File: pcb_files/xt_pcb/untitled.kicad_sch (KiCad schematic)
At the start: 181 parts, among them SW1 SW_Push, SW10 SW_Push, SW11 SW_Push, SW12 SW_Push, SW13 SW_Push, SW14 SW_Push, SW15 SW_Push, SW16 SW_Push, SW17 SW_Push, SW19 SW_Push, SW2 SW_Push, SW20 SW_Push, SW21 SW_Push, SW22 SW_Push, SW23 SW_Push, SW24 SW_Push, SW25 SW_Push, SW26 SW_Push, SW27 SW_Push, SW28 SW_Push, SW29 SW_Push, SW3 SW_Push, SW30 SW_Push, SW31 SW_Push, SW32 SW_Push, SW33 SW_Push, SW34 SW_Push, SW35 SW_Push, SW36 SW_Push, SW37 SW_Push, SW38 SW_Push, SW39 SW_Push, SW4 SW_Push, SW40 SW_Push, SW41 SW_Push, SW42 SW_Push, SW43 SW_Push, SW44 SW_Push, SW45 SW_Push, SW46 SW_Push, SW47 SW_Push, SW48 SW_Push, SW49 SW_Push, SW5 SW_Push, SW50 SW_Push, SW51 SW_Push, SW52 SW_Push, SW53 SW_Push, SW54 SW_Push, SW55 SW_Push, SW56 SW_Push, SW57 SW_Push, SW58 SW_Push, SW59 SW_Push, SW6 SW_Push, SW60 SW_Push, SW61 SW_Push, SW62 SW_Push, SW63 SW_Push, SW64 SW_Push, SW66 SW_Push, SW67 SW_Push, SW68 SW_Push, SW69 SW_Push, SW7 SW_Push, SW70 SW_Push, SW71 SW_Push, SW72 SW_Push, SW73 SW_Push, SW74 SW_Push, SW75 SW_Push, SW76 SW_Push, SW77 SW_Push, SW78 SW_Push, SW79 SW_Push, SW8 SW_Push, SW80 SW_Push, SW81 SW_Push, SW82 SW_Push, SW83 SW_Push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

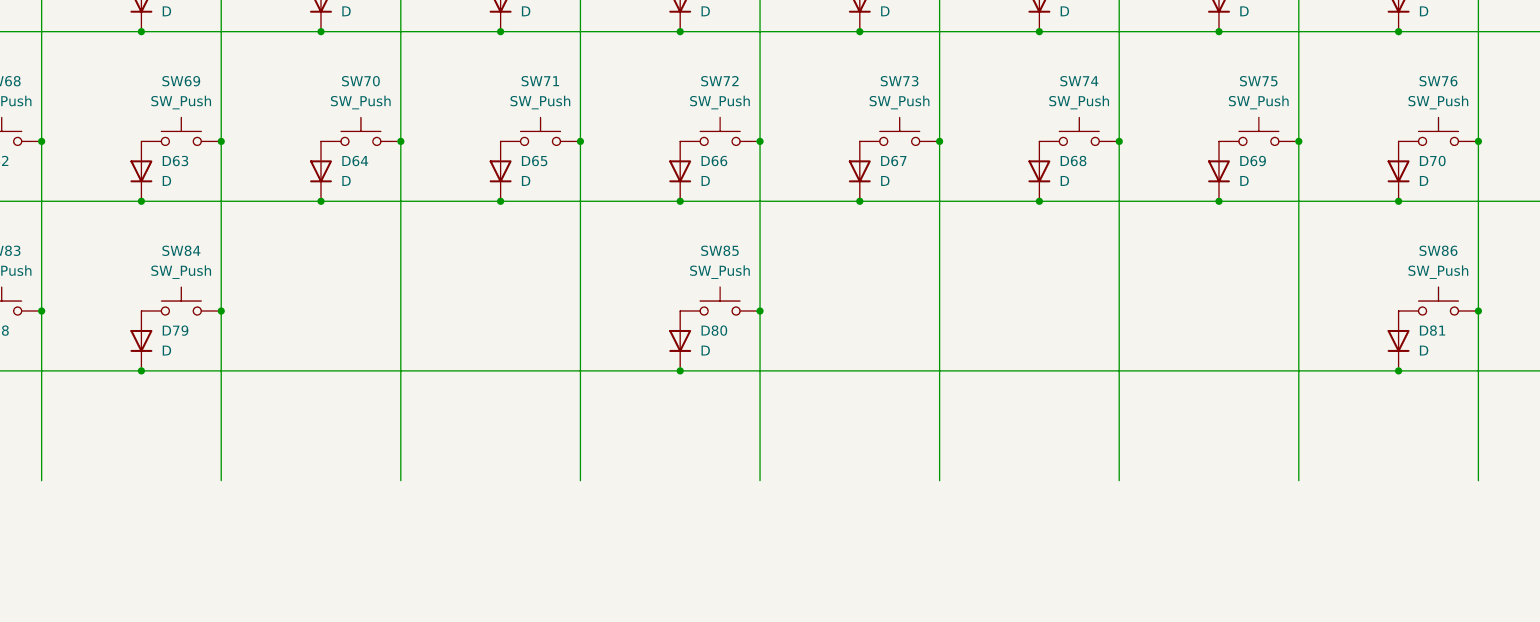
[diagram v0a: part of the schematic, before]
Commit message: new RP2040 pcb
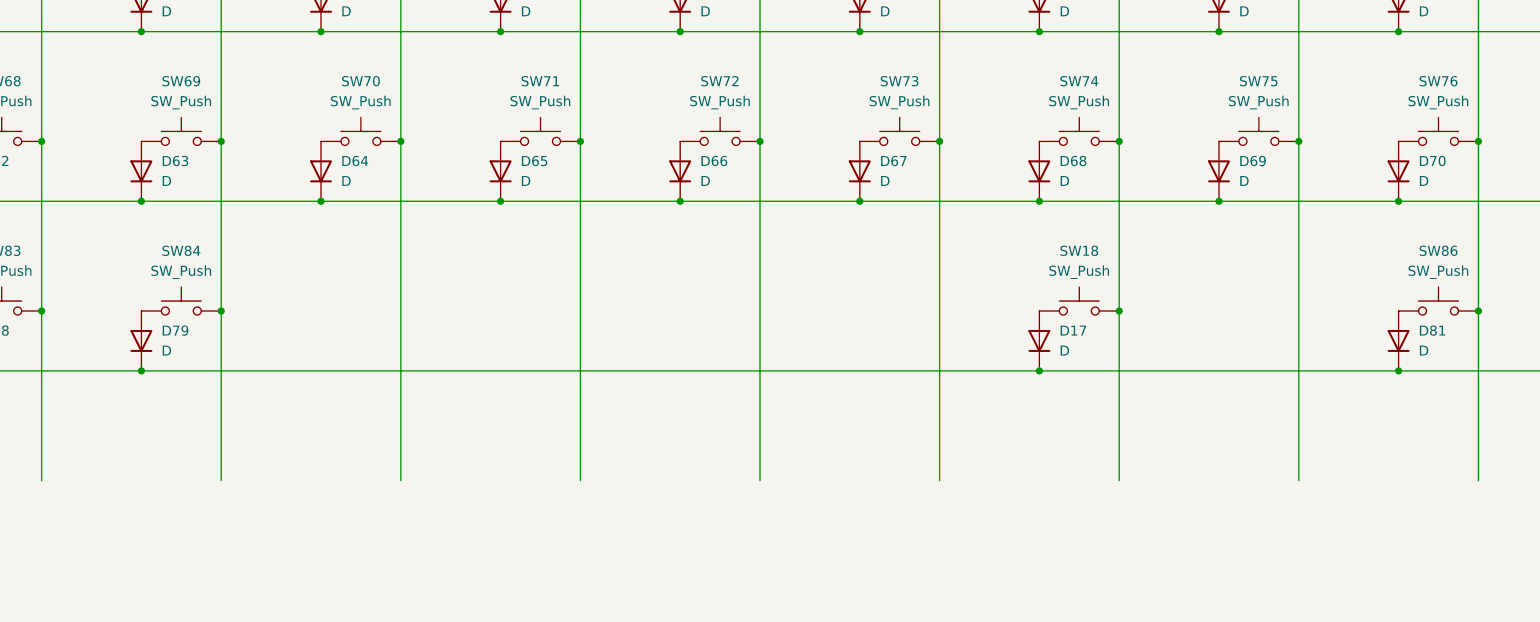
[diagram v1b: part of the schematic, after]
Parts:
- removed D80: D, Diode_SMD:D_SOD-123, symbol Device:D
- removed SW85: SW_Push, PCM_Switch_Keyboard_Hotswap_Kailh:SW_Hotswap_Kailh_MX_Plated_6.25u, symbol Switch:SW_Push
- added D17: D, Diode_SMD:D_SOD-123, symbol Device:D
- added SW18: SW_Push, PCM_Switch_Keyboard_Hotswap_Kailh:SW_Hotswap_Kailh_MX_Plated_6.25u, symbol Switch:SW_Push
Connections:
- net C10: now also SW18.2
- net R5: now also D17.1 (K)
- new net: D17.2 (A), SW18.1
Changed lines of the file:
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@@
 	)
 	(junction
+		(at 281.94 223.52)
+		(diameter 0)
+		(color 0 0 0 0)
+	)
+	(junction
 		(at 373.38 201.93)
 		(diameter 0)
@@
 	)
 	(junction
+		(at 292.1 215.9)
+		(diameter 0)
+		(color 0 0 0 0)
+	)
+	(junction
 		(at 269.24 128.27)
 		(diameter 0)
@@
 	)
 	(junction
-		(at 236.22 223.52)
-		(diameter 0)
-		(color 0 0 0 0)
-	)
-	(junction
 		(at 360.68 128.27)
 		(diameter 0)
@@
 	)
 	(junction
-		(at 246.38 215.9)
-		(diameter 0)
-		(color 0 0 0 0)
-	)
-	(junction
 		(at 510.54 223.52)
 		(diameter 0)
@@
 	(wire
 		(pts
-			(xy 167.64 223.52) (xy 236.22 223.52)
+			(xy 167.64 223.52) (xy 281.94 223.52)
 		)
 		(stroke
@@
 	(wire
 		(pts
+			(xy 292.1 215.9) (xy 292.1 237.49)
+		)
+		(stroke
+			(width 0)
+			(type default)
+		)
+	)
+	(wire
+		(pts
 			(xy 144.78 137.16) (xy 167.64 137.16)
 		)
@@
 	(wire
 		(pts
-			(xy 236.22 223.52) (xy 327.66 223.52)
-		)
-		(stroke
-			(width 0)
-			(type default)
-		)
-	)
-	(wire
-		(pts
 			(xy 91.44 215.9) (xy 91.44 237.49)
 		)
@@
 	(wire
 		(pts
-			(xy 246.38 215.9) (xy 246.38 237.49)
+			(xy 246.38 194.31) (xy 246.38 237.49)
 		)
 		(stroke
@@
 	(wire
 		(pts
-			(xy 292.1 194.31) (xy 292.1 237.49)
+			(xy 292.1 194.31) (xy 292.1 215.9)
 		)
 		(stroke
@@
 	(wire
 		(pts
-			(xy 246.38 194.31) (xy 246.38 215.9)
-		)
-		(stroke
-			(width 0)
-			(type default)
-		)
-	)
-	(wire
-		(pts
 			(xy 121.92 171.45) (xy 121.92 172.72)
 		)
@@
 	(wire
 		(pts
+			(xy 281.94 223.52) (xy 327.66 223.52)
+		)
+		(stroke
+			(width 0)
+			(type default)
+		)
+	)
+	(wire
+		(pts
 			(xy 350.52 137.16) (xy 373.38 137.16)
 		)
@@
 	)
 	(symbol
-		(lib_id "Device:D")
-		(at 236.22 219.71 90)
-		(unit 1)
-		(exclude_from_sim no)
-		(in_bom yes)
-		(on_board yes)
-		(dnp no)
-		(fields_autoplaced yes)
-		(property "Reference" "D80"
-			(at 238.76 218.44 90)
-			(effects
-				(font
-					(size 1.27 1.27)
-				)
-				(justify right)
-			)
-		)
-		(property "Value" "D"
-			(at 238.76 220.98 90)
-			(effects
-				(font
-					(size 1.27 1.27)
-				)
-				(justify right)
-			)
-		)
-		(property "Footprint" "Diode_SMD:D_SOD-123"
-			(at 236.22 219.71 0)
-			(effects
-				(font
-					(size 1.27 1.27)
-				)
-				(hide yes)
-			)
-		)
-		(property "Datasheet" "~"
-			(at 236.22 219.71 0)
-			(effects
-				(font
-					(size 1.27 1.27)
-				)
-				(hide yes)
-			)
-		)
-		(property "Description" "Diode"
-			(at 236.22 219.71 0)
-			(effects
-				(font
-					(size 1.27 1.27)
-				)
-				(hide yes)
-			)
-		)
-		(property "Sim.Device" "D"
-			(at 236.22 219.71 0)
-			(effects
-				(font
-					(size 1.27 1.27)
-				)
-				(hide yes)
-			)
-		)
-		(property "Sim.Pins" "1=K 2=A"
-			(at 236.22 219.71 0)
-			(effects
-				(font
-					(size 1.27 1.27)
-				)
-				(hide yes)
-			)
-		)
-		(pin "2"
-		)
-		(pin "1"
-		)
-		(instances
-			(project "xt_pcb"
-				(path "/0d76ce34-a40d-405c-820f-030fec8e9950/ec63edcb-951a-4690-ae8a-086f997c0dd7"
-					(reference "D80")
-					(unit 1)
-				)
-			)
-		)
-	)
-	(symbol
 		(lib_id "Switch:SW_Push")
 		(at 332.74 151.13 0)
@@
 	)
 	(symbol
+		(lib_id "Switch:SW_Push")
+		(at 287.02 215.9 0)
+		(unit 1)
+		(exclude_from_sim no)
+		(in_bom yes)
+		(on_board yes)
+		(dnp no)
+		(fields_autoplaced yes)
+		(property "Reference" "SW18"
+			(at 287.02 208.28 0)
+			(effects
+				(font
+					(size 1.27 1.27)
+				)
+			)
+		)
+		(property "Value" "SW_Push"
+			(at 287.02 210.82 0)
+			(effects
+				(font
+					(size 1.27 1.27)
+				)
+			)
+		)
+		(property "Footprint" "PCM_Switch_Keyboard_Hotswap_Kailh:SW_Hotswap_Kailh_MX_Plated_6.25u"
+			(at 287.02 210.82 0)
+			(effects
+				(font
+					(size 1.27 1.27)
+				)
+				(hide yes)
+			)
+		)
+		(property "Datasheet" "~"
+			(at 287.02 210.82 0)
+			(effects
+				(font
+					(size 1.27 1.27)
+				)
+				(hide yes)
+			)
+		)
+		(property "Description" "Push button switch, generic, two pins"
+			(at 287.02 215.9 0)
+			(effects
+				(font
+					(size 1.27 1.27)
+				)
+				(hide yes)
+			)
+		)
+		(pin "1"
+		)
+		(pin "2"
+		)
+		(instances
+			(project "xt_pcb"
+				(path "/0d76ce34-a40d-405c-820f-030fec8e9950/ec63edcb-951a-4690-ae8a-086f997c0dd7"
+					(reference "SW18")
+					(unit 1)
+				)
+			)
+		)
+	)
+	(symbol
 		(lib_id "Device:D")
 		(at 533.4 219.71 90)
@@
 	)
 	(symbol
+		(lib_id "Device:D")
+		(at 281.94 219.71 90)
+		(unit 1)
+		(exclude_from_sim no)
+		(in_bom yes)
+		(on_board yes)
+		(dnp no)
+		(fields_autoplaced yes)
+		(property "Reference" "D17"
+			(at 284.48 218.44 90)
+			(effects
+				(font
+					(size 1.27 1.27)
+				)
+				(justify right)
+			)
+		)
+		(property "Value" "D"
+			(at 284.48 220.98 90)
+			(effects
+				(font
+					(size 1.27 1.27)
+				)
+				(justify right)
+			)
+		)
+		(property "Footprint" "Diode_SMD:D_SOD-123"
+			(at 281.94 219.71 0)
+			(effects
+				(font
+					(size 1.27 1.27)
+				)
+				(hide yes)
+			)
+		)
+		(property "Datasheet" "~"
+			(at 281.94 219.71 0)
+			(effects
+				(font
+					(size 1.27 1.27)
+				)
+				(hide yes)
+			)
+		)
+		(property "Description" "Diode"
+			(at 281.94 219.71 0)
+			(effects
+				(font
+					(size 1.27 1.27)
+				)
+				(hide yes)
+			)
+		)
+		(property "Sim.Device" "D"
+			(at 281.94 219.71 0)
+			(effects
+				(font
+					(size 1.27 1.27)
+				)
+				(hide yes)
+			)
+		)
+		(property "Sim.Pins" "1=K 2=A"
+			(at 281.94 219.71 0)
+			(effects
+				(font
+					(size 1.27 1.27)
+				)
+				(hide yes)
+			)
+		)
+		(pin "2"
+		)
+		(pin "1"
+		)
+		(instances
+			(project "xt_pcb"
+				(path "/0d76ce34-a40d-405c-820f-030fec8e9950/ec63edcb-951a-4690-ae8a-086f997c0dd7"
+					(reference "D17")
+					(unit 1)
+				)
+			)
+		)
+	)
+	(symbol
 		(lib_id "Switch:SW_Push")
 		(at 127 172.72 0)
@@
 					(unit 1)
 				)
-			)
-		)
-	)
-	(symbol
-		(lib_id "Switch:SW_Push")
-		(at 241.3 215.9 0)
-		(unit 1)
-		(exclude_from_sim no)
-		(in_bom yes)
-		(on_board yes)
-		(dnp no)
-		(fields_autoplaced yes)
-		(property "Reference" "SW85"
-			(at 241.3 208.28 0)
-			(effects
-				(font
-					(size 1.27 1.27)
-				)
-			)
-		)
-		(property "Value" "SW_Push"
-			(at 241.3 210.82 0)
-			(effects
-				(font
-					(size 1.27 1.27)
-				)
-			)
-		)
-		(property "Footprint" "PCM_Switch_Keyboard_Hotswap_Kailh:SW_Hotswap_Kailh_MX_Plated_6.25u"
-			(at 241.3 210.82 0)
-			(effects
-				(font
-					(size 1.27 1.27)
-				)
-				(hide yes)
-			)
-		)
-		(property "Datasheet" "~"
-			(at 241.3 210.82 0)
-			(effects
-				(font
-					(size 1.27 1.27)
-				)
-				(hide yes)
-			)
-		)
-		(property "Description" "Push button switch, generic, two pins"
-			(at 241.3 215.9 0)
-			(effects
-				(font
-					(size 1.27 1.27)
-				)
-				(hide yes)
-			)
-		)
-		(pin "1"
-		)
-		(pin "2"
-		)
-		(instances
-			(project "xt_pcb"
-				(path "/0d76ce34-a40d-405c-820f-030fec8e9950/ec63edcb-951a-4690-ae8a-086f997c0dd7"
-					(reference "SW85")
-					(unit 1)
-				)
